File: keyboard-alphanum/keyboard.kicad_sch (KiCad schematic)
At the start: 173 parts, among them J1 USB_B_Mini, U1 ATmega168PA-A, U2 CH340C, U3 74HC154D, U4 74HC4051, Y1 16MHz

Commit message: Keyboard alphanum v1.0
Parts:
- removed D11, D12, D13, D18, D19, D20, D21, D25, D26, D27, D28, D32, D33, D34, D35, D36, D37, D38, D39, D40, D41, D42, D43, D44, D45, D46, D47, D48, D49, D5, D50, D51, D52, D53, D54, D55, D56, D57, D58, D59, D6, D60, D61, D62, D63, D64, D65, D66, D67, D68, D69, D70, D71, D72, D73, D74, D75, D76, D77: D, common:D_0603_1608Metric, symbol symbols:D
- removed R10, R8, R9: 1K, common:R_0603_1608Metric, symbol symbols:R
- removed S11: K, Switch_Keyboard_Cherry_MX:SW_Cherry_MX_PCB_1.00u, symbol symbols:Switch
- removed S12: M, Switch_Keyboard_Cherry_MX:SW_Cherry_MX_PCB_1.00u, symbol symbols:Switch
- removed S13: Rctrl, Switch_Keyboard_Cherry_MX:SW_Cherry_MX_PCB_1.00u, symbol symbols:Switch
- removed S17, S19, S24, S25, S26, S31, S32, S33: sym, Switch_Keyboard_Cherry_MX:SW_Cherry_MX_PCB_1.00u, symbol symbols:Switch
- removed S18: L, Switch_Keyboard_Cherry_MX:SW_Cherry_MX_PCB_1.00u, symbol symbols:Switch
- removed S20: Aleft, Switch_Keyboard_Cherry_MX:SW_Cherry_MX_PCB_1.00u, symbol symbols:Switch
- removed S27: Adown, Switch_Keyboard_Cherry_MX:SW_Cherry_MX_PCB_1.00u, symbol symbols:Switch
- removed S34: Aright, Switch_Keyboard_Cherry_MX:SW_Cherry_MX_PCB_1.00u, symbol symbols:Switch
- removed S35: F5, Switch_Keyboard_Cherry_MX:SW_Cherry_MX_PCB_1.00u, symbol symbols:Switch
- removed S36: 4, Switch_Keyboard_Cherry_MX:SW_Cherry_MX_PCB_1.00u, symbol symbols:Switch
- removed S37: W, Switch_Keyboard_Cherry_MX:SW_Cherry_MX_PCB_1.00u, symbol symbols:Switch
- removed S38: CL, Switch_Keyboard_Cherry_MX:SW_Cherry_MX_PCB_1.00u, symbol symbols:Switch
- removed S39: enter, Switch_Keyboard_Cherry_MX:SW_Cherry_MX_PCB_2.00u, symbol symbols:Switch
- removed S40: Rshift, Switch_Keyboard_Cherry_MX:SW_Cherry_MX_PCB_1.00u, symbol symbols:Switch
- removed S41: F6, Switch_Keyboard_Cherry_MX:SW_Cherry_MX_PCB_1.00u, symbol symbols:Switch
- removed S42: 5, Switch_Keyboard_Cherry_MX:SW_Cherry_MX_PCB_1.00u, symbol symbols:Switch
- removed S43: E, Switch_Keyboard_Cherry_MX:SW_Cherry_MX_PCB_1.00u, symbol symbols:Switch
- removed S44: A, Switch_Keyboard_Cherry_MX:SW_Cherry_MX_PCB_1.00u, symbol symbols:Switch
- removed S45: Lshift, Switch_Keyboard_Cherry_MX:SW_Cherry_MX_PCB_1.00u, symbol symbols:Switch
- removed S46: Atop, Switch_Keyboard_Cherry_MX:SW_Cherry_MX_PCB_1.00u, symbol symbols:Switch
- removed S47: F7, Switch_Keyboard_Cherry_MX:SW_Cherry_MX_PCB_1.00u, symbol symbols:Switch
- removed S48: 6, Switch_Keyboard_Cherry_MX:SW_Cherry_MX_PCB_1.00u, symbol symbols:Switch
- removed S49: R, Switch_Keyboard_Cherry_MX:SW_Cherry_MX_PCB_1.00u, symbol symbols:Switch
- removed S5: J, Switch_Keyboard_Cherry_MX:SW_Cherry_MX_PCB_1.00u, symbol symbols:Switch
- removed S50: S, Switch_Keyboard_Cherry_MX:SW_Cherry_MX_PCB_1.00u, symbol symbols:Switch
- removed S51: Z, Switch_Keyboard_Cherry_MX:SW_Cherry_MX_PCB_1.00u, symbol symbols:Switch
- removed S52: Lctrl, Switch_Keyboard_Cherry_MX:SW_Cherry_MX_PCB_1.00u, symbol symbols:Switch
- removed S53: F8, Switch_Keyboard_Cherry_MX:SW_Cherry_MX_PCB_1.00u, symbol symbols:Switch
- removed S54: 7, Switch_Keyboard_Cherry_MX:SW_Cherry_MX_PCB_1.00u, symbol symbols:Switch
- removed S55: T, Switch_Keyboard_Cherry_MX:SW_Cherry_MX_PCB_1.00u, symbol symbols:Switch
- removed S56: D, Switch_Keyboard_Cherry_MX:SW_Cherry_MX_PCB_1.00u, symbol symbols:Switch
- removed S57: X, Switch_Keyboard_Cherry_MX:SW_Cherry_MX_PCB_1.00u, symbol symbols:Switch
- removed S58: Lwin, Switch_Keyboard_Cherry_MX:SW_Cherry_MX_PCB_1.00u, symbol symbols:Switch
- removed S59: F9, Switch_Keyboard_Cherry_MX:SW_Cherry_MX_PCB_1.00u, symbol symbols:Switch
- removed S6: N, Switch_Keyboard_Cherry_MX:SW_Cherry_MX_PCB_1.00u, symbol symbols:Switch
- removed S60: 8, Switch_Keyboard_Cherry_MX:SW_Cherry_MX_PCB_1.00u, symbol symbols:Switch
- removed S61: Y, Switch_Keyboard_Cherry_MX:SW_Cherry_MX_PCB_1.00u, symbol symbols:Switch
- removed S62: F, Switch_Keyboard_Cherry_MX:SW_Cherry_MX_PCB_1.00u, symbol symbols:Switch
- removed S63: C, Switch_Keyboard_Cherry_MX:SW_Cherry_MX_PCB_1.00u, symbol symbols:Switch
- removed S64: Lalt, Switch_Keyboard_Cherry_MX:SW_Cherry_MX_PCB_1.00u, symbol symbols:Switch
- removed S65: F10, Switch_Keyboard_Cherry_MX:SW_Cherry_MX_PCB_1.00u, symbol symbols:Switch
- removed S66: 9, Switch_Keyboard_Cherry_MX:SW_Cherry_MX_PCB_1.00u, symbol symbols:Switch
- removed S67: U, Switch_Keyboard_Cherry_MX:SW_Cherry_MX_PCB_1.00u, symbol symbols:Switch
- removed S68: G, Switch_Keyboard_Cherry_MX:SW_Cherry_MX_PCB_1.00u, symbol symbols:Switch
- removed S69: V, Switch_Keyboard_Cherry_MX:SW_Cherry_MX_PCB_1.00u, symbol symbols:Switch
- removed S70: space, Switch_Keyboard_Cherry_MX:SW_Cherry_MX_PCB_6.00u, symbol symbols:Switch
- removed S71: F11, Switch_Keyboard_Cherry_MX:SW_Cherry_MX_PCB_1.00u, symbol symbols:Switch
- removed S72: 0, Switch_Keyboard_Cherry_MX:SW_Cherry_MX_PCB_1.00u, symbol symbols:Switch
- removed S73: I, Switch_Keyboard_Cherry_MX:SW_Cherry_MX_PCB_1.00u, symbol symbols:Switch
- removed S74: H, Switch_Keyboard_Cherry_MX:SW_Cherry_MX_PCB_1.00u, symbol symbols:Switch
- removed S75: B, Switch_Keyboard_Cherry_MX:SW_Cherry_MX_PCB_1.00u, symbol symbols:Switch
- removed S76: Ralt, Switch_Keyboard_Cherry_MX:SW_Cherry_MX_PCB_1.00u, symbol symbols:Switch
- removed U3: 74HC154D, common:SSOP-24_3.9x8.7mm_P0.635mm, symbol symbols:74HC154D
- removed U4: 74HC4051, common:SSOP-16_3.9x4.9mm_P0.635mm, symbol symbols:74HC4051
- added D1: LED, common:LED_1206_3216Metric, symbol symbols:LED
- added R2: 1K, common:R_0603_1608Metric, symbol symbols:R
- S1: value Esc -> NL
- S10: renamed from S15; value 1 -> plus; footprint Switch_Keyboard_Cherry_MX:SW_Cherry_MX_PCB_1.00u -> Switch_Keyboard_Cherry_MX:SW_Cherry_MX_PCB_2.00u_90deg
- S11: renamed from S16; value BS -> 2
- S12: renamed from S21; value F3 -> sub
- S13: renamed from S22; value 2 -> 4
- S14: renamed from S23; value tab -> 3
- S15: renamed from S28; value F4 -> 7
- S16: renamed from S29; value 3 -> 5
- S17: renamed from S30; value Q -> enter; footprint Switch_Keyboard_Cherry_MX:SW_Cherry_MX_PCB_1.00u -> Switch_Keyboard_Cherry_MX:SW_Cherry_MX_PCB_2.00u_90deg
- S2: value F12 -> 8
- S3: value sym -> 6
- S4: value O -> 0; footprint Switch_Keyboard_Cherry_MX:SW_Cherry_MX_PCB_1.00u -> Switch_Keyboard_Cherry_MX:SW_Cherry_MX_PCB_2.00u
- S5: renamed from S7; value F1 -> div
- S6: renamed from S8; value sym -> 9
- S7: renamed from S9; value sym -> 1
- S8: renamed from S10; value P -> point
- S9: renamed from S14; value F2 -> mul
- renumbered D15 to D11, D16 to D12, D17 to D13, D22 to D14, D23 to D15, D24 to D16, D29 to D17, D30 to D18, D31 to D19, D1 to D2, D2 to D3, D3 to D4, D4 to D5, D14 to D6, R2 to R3, R3 to R4, R4 to R5, R5 to R6, R6 to R7, R7 to R8
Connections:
- net GND: now also R2.2
- net I0: now also U1.28 (PC5)
- net I1: now also U1.1 (PD3)
- net I2: now also U1.2 (PD4)
- net I3: now also U1.9 (PD5)
- net O0: now also U1.23 (PC0)
- net O1: now also U1.24 (PC1)
- net O2: now also U1.25 (PC2)
- net O3: now also U1.26 (PC3)
- net O4: now also U1.27 (PC4)
- net at U1.16 (PB4): now also D1.2 (A)
- new net: D1.1 (K), R2.1
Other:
- title: Arduino Keyboard -> keyboard alphanum
- moved on the sheet: C1, C2, C3, C4, D10, D11, D12, D13, D14, D15, D16, D17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

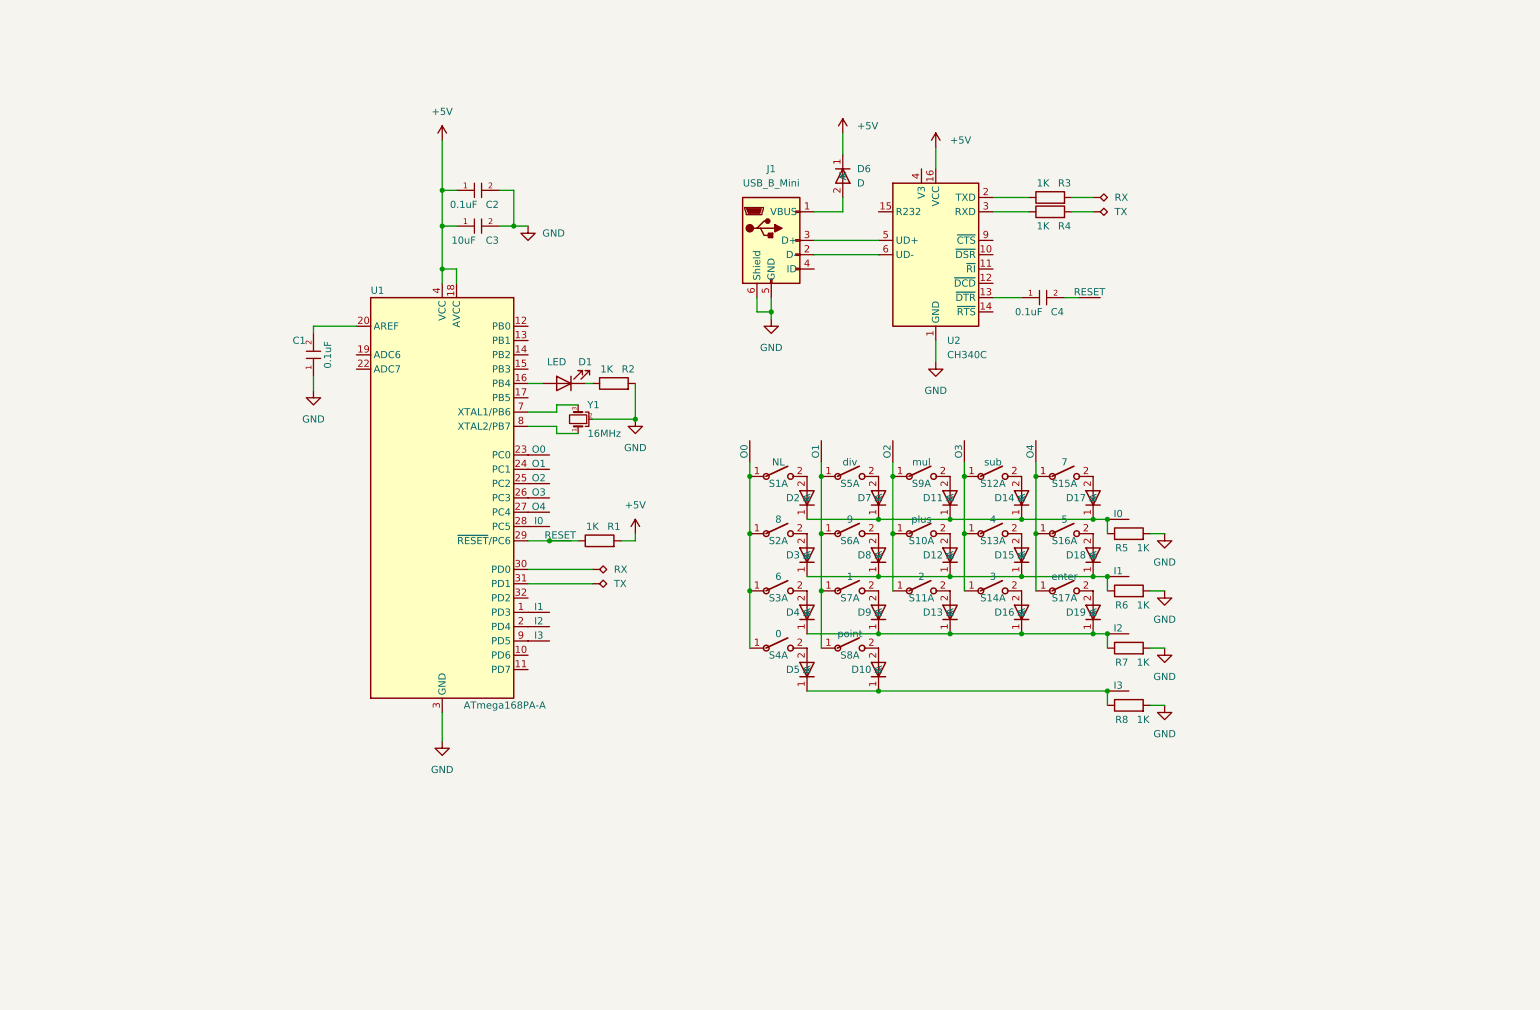
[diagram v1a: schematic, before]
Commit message: Update keyboar pcb design
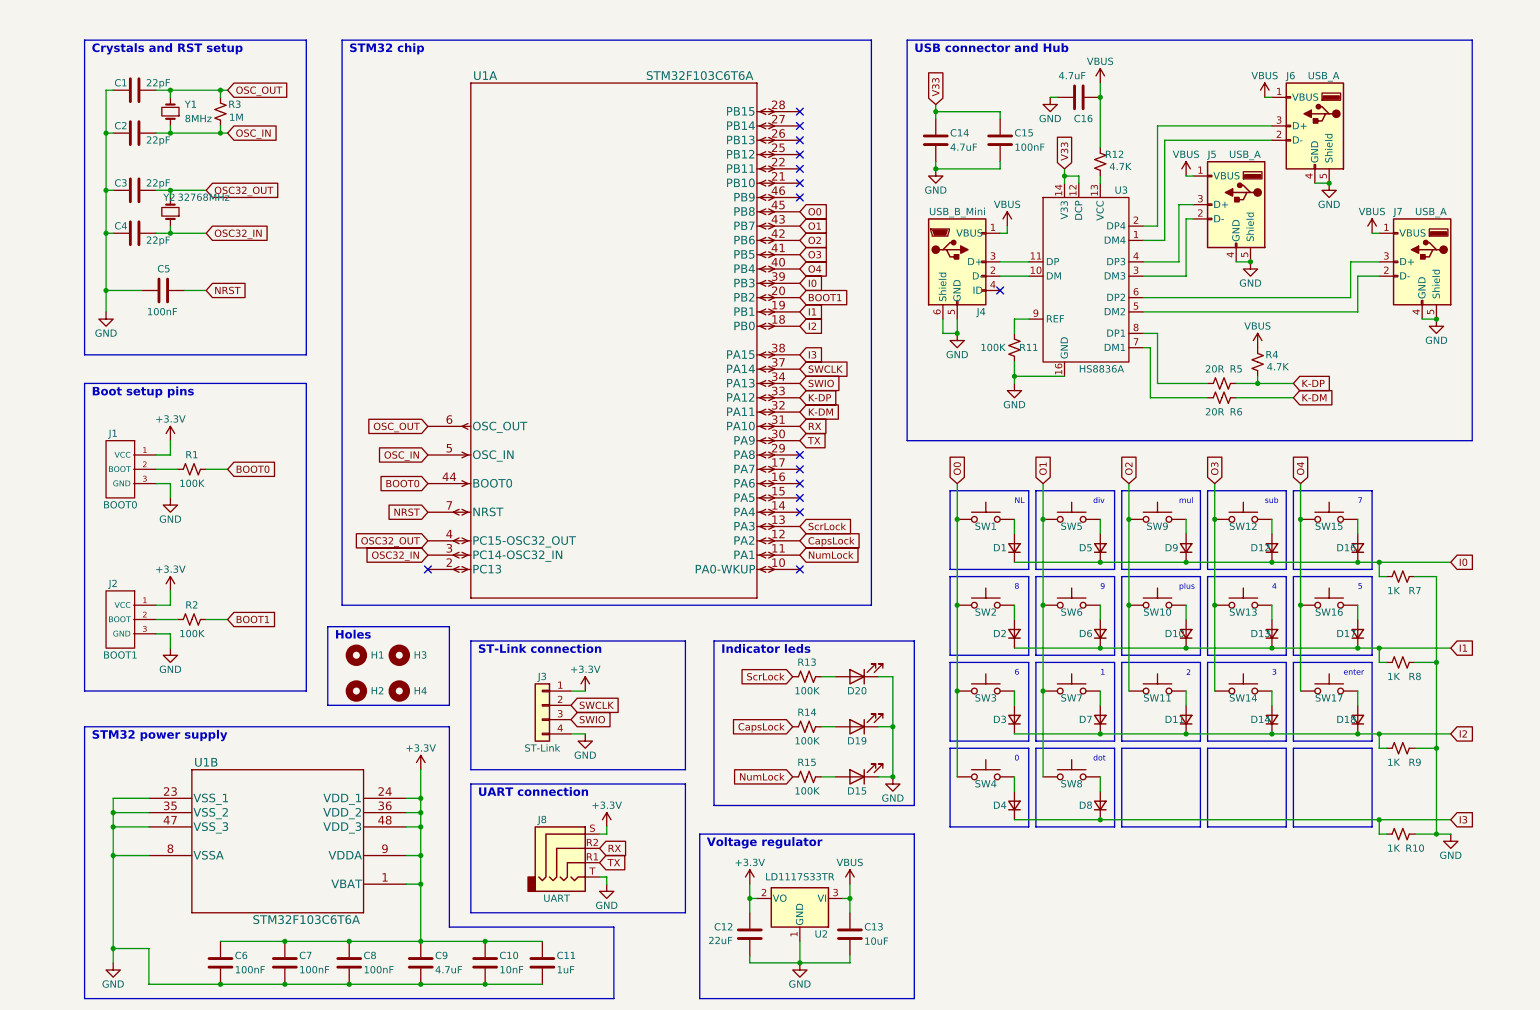
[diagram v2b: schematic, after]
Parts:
- removed C1, C2, C4: 0.1uF, common:C_1206_3216Metric, symbol symbols:C
- removed C3: 10uF, common:C_1206_3216Metric, symbol symbols:C
- removed D1: LED, common:LED_1206_3216Metric, symbol symbols:LED
- removed D10, D11, D12, D13, D14, D15, D16, D17, D18, D19, D2, D3, D4, D5, D6, D7, D8, D9: D, common:D_0603_1608Metric, symbol symbols:D
- removed R1, R2, R3, R4, R5, R6, R7, R8: 1K, common:R_0603_1608Metric, symbol symbols:R
- removed S1: NL, Switch_Keyboard_Cherry_MX:SW_Cherry_MX_PCB_1.00u, symbol symbols:Switch
- removed S10: plus, Switch_Keyboard_Cherry_MX:SW_Cherry_MX_PCB_2.00u_90deg, symbol symbols:Switch
- removed S11: 2, Switch_Keyboard_Cherry_MX:SW_Cherry_MX_PCB_1.00u, symbol symbols:Switch
- removed S12: sub, Switch_Keyboard_Cherry_MX:SW_Cherry_MX_PCB_1.00u, symbol symbols:Switch
- removed S13: 4, Switch_Keyboard_Cherry_MX:SW_Cherry_MX_PCB_1.00u, symbol symbols:Switch
- removed S14: 3, Switch_Keyboard_Cherry_MX:SW_Cherry_MX_PCB_1.00u, symbol symbols:Switch
- removed S15: 7, Switch_Keyboard_Cherry_MX:SW_Cherry_MX_PCB_1.00u, symbol symbols:Switch
- removed S16: 5, Switch_Keyboard_Cherry_MX:SW_Cherry_MX_PCB_1.00u, symbol symbols:Switch
- removed S17: enter, Switch_Keyboard_Cherry_MX:SW_Cherry_MX_PCB_2.00u_90deg, symbol symbols:Switch
- removed S2: 8, Switch_Keyboard_Cherry_MX:SW_Cherry_MX_PCB_1.00u, symbol symbols:Switch
- removed S3: 6, Switch_Keyboard_Cherry_MX:SW_Cherry_MX_PCB_1.00u, symbol symbols:Switch
- removed S4: 0, Switch_Keyboard_Cherry_MX:SW_Cherry_MX_PCB_2.00u, symbol symbols:Switch
- removed S5: div, Switch_Keyboard_Cherry_MX:SW_Cherry_MX_PCB_1.00u, symbol symbols:Switch
- removed S6: 9, Switch_Keyboard_Cherry_MX:SW_Cherry_MX_PCB_1.00u, symbol symbols:Switch
- removed S7: 1, Switch_Keyboard_Cherry_MX:SW_Cherry_MX_PCB_1.00u, symbol symbols:Switch
- removed S8: point, Switch_Keyboard_Cherry_MX:SW_Cherry_MX_PCB_1.00u, symbol symbols:Switch
- removed S9: mul, Switch_Keyboard_Cherry_MX:SW_Cherry_MX_PCB_1.00u, symbol symbols:Switch
- removed U1: ATmega168PA-A, Package_QFP:TQFP-32_7x7mm_P0.8mm, symbol symbols:ATmega168PA-A
- removed U2: CH340C, Package_SO:SOIC-16_3.9x9.9mm_P1.27mm, symbol symbols:CH340C
- removed Y1: 16MHz, common:Resonator_SMD_Murata_CSTxExxV-3Pin_3.0x1.1mm, symbol symbols:Crystal_GND2_Small
- added C1, C2, C3, C4: 22pF, Capacitor_SMD:C_0805_2012Metric, symbol Device:C
- added C10: 10nF, Capacitor_SMD:C_0805_2012Metric, symbol Device:C
- added C11: 1uF, Capacitor_SMD:C_0805_2012Metric, symbol Device:C
- added C12: 22uF, Capacitor_SMD:C_1206_3216Metric, symbol Device:C
- added C13: 10uF, Capacitor_SMD:C_1206_3216Metric, symbol Device:C
- added C14, C16, C9: 4.7uF, Capacitor_SMD:C_0805_2012Metric, symbol Device:C
- added C15, C5, C6, C7, C8: 100nF, Capacitor_SMD:C_0805_2012Metric, symbol Device:C
- added D1, D10, D11, D12, D13, D14, D16, D17, D18, D2, D3, D4, D5, D6, D7, D8, D9: D_Small, Diode_SMD:D_SOD-323, symbol Device:D_Small
- added D15: NumLock, LED_THT:LED_D5.0mm, symbol Device:LED
- added D19: CapsLock, LED_THT:LED_D5.0mm, symbol Device:LED
- added D20: ScrollLock, LED_THT:LED_D5.0mm, symbol Device:LED
- added H1, H2, H3, H4: MountingHole, symbol Mechanical:MountingHole
- added J1: BOOT0, Jumper:SolderJumper-3_P1.3mm_Open_RoundedPad1.0x1.5mm, symbol symbols:boot_pins
- added J2: BOOT1, Jumper:SolderJumper-3_P1.3mm_Open_RoundedPad1.0x1.5mm, symbol symbols:boot_pins
- added J3: ST-Link, Connector_PinHeader_2.54mm:PinHeader_1x04_P2.54mm_Vertical, symbol Connector_Generic:Conn_01x04
- added J5, J6, J7: USB_A, common:USB_A_Molex_105057_Vertical, symbol Connector:USB_A
- added J8: UART, common:PJ320D, symbol Connector:AudioJack4
- added R1, R11, R13, R14, R15, R2: 100K, Resistor_SMD:R_0805_2012Metric, symbol Device:R_Small_US
- added R10, R7, R8, R9: 1K, Resistor_SMD:R_0805_2012Metric, symbol Device:R_Small_US
- added R12, R4: 4.7K, Resistor_SMD:R_0805_2012Metric, symbol Device:R_Small_US
- added R3: 1M, Resistor_SMD:R_0805_2012Metric, symbol Device:R_Small_US
- added R5, R6: 20R, Resistor_SMD:R_0805_2012Metric, symbol Device:R_Small_US
- added SW1: NL, Switch_Keyboard_Cherry_MX:SW_Cherry_MX_PCB_1.00u, symbol Switch:SW_Push
- added SW10: plus, Switch_Keyboard_Cherry_MX:SW_Cherry_MX_PCB_2.00u_90deg, symbol Switch:SW_Push
- added SW11: 2, Switch_Keyboard_Cherry_MX:SW_Cherry_MX_PCB_1.00u, symbol Switch:SW_Push
- added SW12: sub, Switch_Keyboard_Cherry_MX:SW_Cherry_MX_PCB_1.00u, symbol Switch:SW_Push
- added SW13: 4, Switch_Keyboard_Cherry_MX:SW_Cherry_MX_PCB_1.00u, symbol Switch:SW_Push
- added SW14: 3, Switch_Keyboard_Cherry_MX:SW_Cherry_MX_PCB_1.00u, symbol Switch:SW_Push
- added SW15: 7, Switch_Keyboard_Cherry_MX:SW_Cherry_MX_PCB_1.00u, symbol Switch:SW_Push
- added SW16: 5, Switch_Keyboard_Cherry_MX:SW_Cherry_MX_PCB_1.00u, symbol Switch:SW_Push
- added SW17: enter, Switch_Keyboard_Cherry_MX:SW_Cherry_MX_PCB_2.00u_90deg, symbol Switch:SW_Push
- added SW2: 8, Switch_Keyboard_Cherry_MX:SW_Cherry_MX_PCB_1.00u, symbol Switch:SW_Push
- added SW3: 6, Switch_Keyboard_Cherry_MX:SW_Cherry_MX_PCB_1.00u, symbol Switch:SW_Push
- added SW4: 0, Switch_Keyboard_Cherry_MX:SW_Cherry_MX_PCB_2.00u, symbol Switch:SW_Push
- added SW5: div, Switch_Keyboard_Cherry_MX:SW_Cherry_MX_PCB_1.00u, symbol Switch:SW_Push
- added SW6: 9, Switch_Keyboard_Cherry_MX:SW_Cherry_MX_PCB_1.00u, symbol Switch:SW_Push
- added SW7: 1, Switch_Keyboard_Cherry_MX:SW_Cherry_MX_PCB_1.00u, symbol Switch:SW_Push
- added SW8: dot, Switch_Keyboard_Cherry_MX:SW_Cherry_MX_PCB_1.00u, symbol Switch:SW_Push
- added SW9: mul, Switch_Keyboard_Cherry_MX:SW_Cherry_MX_PCB_1.00u, symbol Switch:SW_Push
- added U1: STM32F103C6T6A, symbol STM32F103C6T6A:STM32F103C6T6A
- added U2: LD1117S33TR, Package_TO_SOT_SMD:SOT-223-3_TabPin2, symbol Regulator_Linear:LD1117S33TR_SOT223
- added U3: HS8836A, Package_SO:SOP-16_3.9x9.9mm_P1.27mm, symbol symbols:HS8836A
- added Y1: 8MHz, Crystal:Crystal_SMD_Abracon_ABM3-2Pin_5.0x3.2mm, symbol Device:Crystal_Small
- added Y2: 32768MHz, Crystal:Crystal_SMD_SeikoEpson_MC306-4Pin_8.0x3.2mm, symbol Device:Crystal_Small
- J4: renamed from J1; footprint common:USB_Micro-B_GCT_USB3076-30-A -> common:USB_Micro-B_A01SB141B1-245
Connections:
- net GND: now also C1.1, C10.2, C11.2, C12.2, C13.2, C14.2, C15.2, C16.1, C2.1, C3.1, C4.1, C5.1, C6.2, C7.2, C8.2, C9.2, D15.1 (K), D19.1 (K), D20.1 (K), J1.3 (GND), J2.3 (GND), J3.4 (Pin_4), J5.4 (GND), J5.5 (Shield), J6.4 (GND), J6.5 (Shield), J7.4 (GND), J7.5 (Shield), J8.T, R10.2, R11.2, R7.2, R8.2, R9.2, U1.23 (VSS_1), U1.35 (VSS_2), U1.47 (VSS_3), U1.8 (VSSA), U2.1 (GND), U3.16 (GND)
- net I0: now also D1.1 (K), D12.1 (K), D16.1 (K), D5.1 (K), D9.1 (K), R7.1, U1.39 (PB3)
- net I1: now also D10.1 (K), D13.1 (K), D17.1 (K), D2.1 (K), D6.1 (K), R8.1, U1.19 (PB1)
- net I2: now also D11.1 (K), D14.1 (K), D18.1 (K), D3.1 (K), D7.1 (K), R9.1, U1.18 (PB0)
- net I3: now also D4.1 (K), D8.1 (K), R10.1, U1.38 (PA15)
- net O0: now also SW1.1, SW2.1, SW3.1, SW4.1, U1.45 (PB8)
- net O1: now also SW5.1, SW6.1, SW7.1, SW8.1, U1.43 (PB7)
- net O2: now also SW10.1, SW11.1, SW9.1, U1.42 (PB6)
- net O3: now also SW12.1, SW13.1, SW14.1, U1.41 (PB5)
- net O4: now also SW15.1, SW16.1, SW17.1, U1.40 (PB4)
- net RX: now also J8.R2, U1.31 (PA10)
- net TX: now also J8.R1, U1.30 (PA9)
- net VBUS: now reaches J4.1 (VBUS)
- net VBUS: now also C13.1, C16.2, J5.1 (VBUS), J6.1 (VBUS), J7.1 (VBUS), R12.2, R4.2, U2.3 (VI)
- net at J4.2 (D-): now also U3.10 (DM)
- net at J4.3 (D+): now also U3.11 (DP)
- new net: D5.2 (A), SW5.2
- new net: D13.2 (A), SW13.2
- new net: D9.2 (A), SW9.2
- new net: D19.2 (A), R14.2
- new net: D2.2 (A), SW2.2
- new net: D8.2 (A), SW8.2
- new net: D3.2 (A), SW3.2
- new net: D4.2 (A), SW4.2
- new net: D11.2 (A), SW11.2
- new net: D20.2 (A), R13.2
- new net: D12.2 (A), SW12.2
- new net: D7.2 (A), SW7.2
- new net: D18.2 (A), SW17.2
- new net: J2.2 (BOOT), R2.1
- new net: D17.2 (A), SW16.2
- new net: J6.2 (D-), U3.1 (DM4)
- new net: R12.1, U3.13 (VCC)
- new net: J6.3 (D+), U3.2 (DP4)
- new net: J5.2 (D-), U3.3 (DM3)
- new net: J5.3 (D+), U3.4 (DP3)
- new net: J7.2 (D-), U3.5 (DM2)
- new net: J7.3 (D+), U3.6 (DP2)
- new net: R6.1, U3.7 (DM1)
- new net: R5.1, U3.8 (DP1)
- new net: R11.1, U3.9 (REF)
- new net: D14.2 (A), SW14.2
- new net: J1.2 (BOOT), R1.1
- new net: D1.2 (A), SW1.2
- new net: D10.2 (A), SW10.2
- new net: D15.2 (A), R15.2
- new net: D16.2 (A), SW15.2
- new net: D6.2 (A), SW6.2
- new net +3.3V: C10.1, C11.1, C12.1, C6.1, C7.1, C8.1, C9.1, J1.1 (VCC), J2.1 (VCC), J3.1 (Pin_1), J8.S, U1.1 (VBAT), U1.24 (VDD_1), U1.36 (VDD_2), U1.48 (VDD_3), U1.9 (VDDA), U2.2 (VO)
- new net BOOT0: R1.2, U1.44 (BOOT0)
- new net BOOT1: R2.2, U1.20 (PB2)
- new net CapsLock: R14.1, U1.12 (PA2)
- new net K-DM: R6.2, U1.32 (PA11)
- new net K-DP: R4.1, R5.2, U1.33 (PA12)
- new net NRST: C5.2, U1.7 (NRST)
- new net NumLock: R15.1, U1.11 (PA1)
- new net OSC32_IN: C4.2, U1.3 (PC14-OSC32_IN), Y2.1
- new net OSC32_OUT: C3.2, U1.4 (PC15-OSC32_OUT), Y2.4
- new net OSC_IN: C2.2, R3.1, U1.5 (OSC_IN), Y1.1
- new net OSC_OUT: C1.2, R3.2, U1.6 (OSC_OUT), Y1.2
- new net SWCLK: J3.2 (Pin_2), U1.37 (PA14)
- new net SWIO: J3.3 (Pin_3), U1.34 (PA13)
- new net ScrLock: R13.1, U1.13 (PA3)
- new net V33: C14.1, C15.1, U3.12 (DCP), U3.14 (V33)
- no-connect marks 0 -> 15
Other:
- note added: "0"
- note added: "1"
- note added: "2"
- note added: "3"
- note added: "4"
- note added: "5"
- note added: "6"
- note added: "7"
- note added: "8"
- note added: "9"
- note added: "Boot setup pins"
- note added: "Crystals and RST setup"
- note added: "Holes"
- note added: "Indicator leds"
- note added: "NL"
- note added: "ST-Link connection"
- note added: "STM32 chip"
- note added: "STM32 power supply"
- note added: "UART connection"
- note added: "USB connector and Hub"
- note added: "Voltage regulator"
- note added: "div"
- note added: "dot"
- note added: "enter"
- note added: "mul"
- note added: "plus"
- note added: "sub"
- moved on the sheet: J4
